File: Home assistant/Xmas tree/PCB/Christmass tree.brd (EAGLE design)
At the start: 64 x 38 mm, 12 parts, among them T1 BC547, X1 3PIN_5MM_TERMINAL

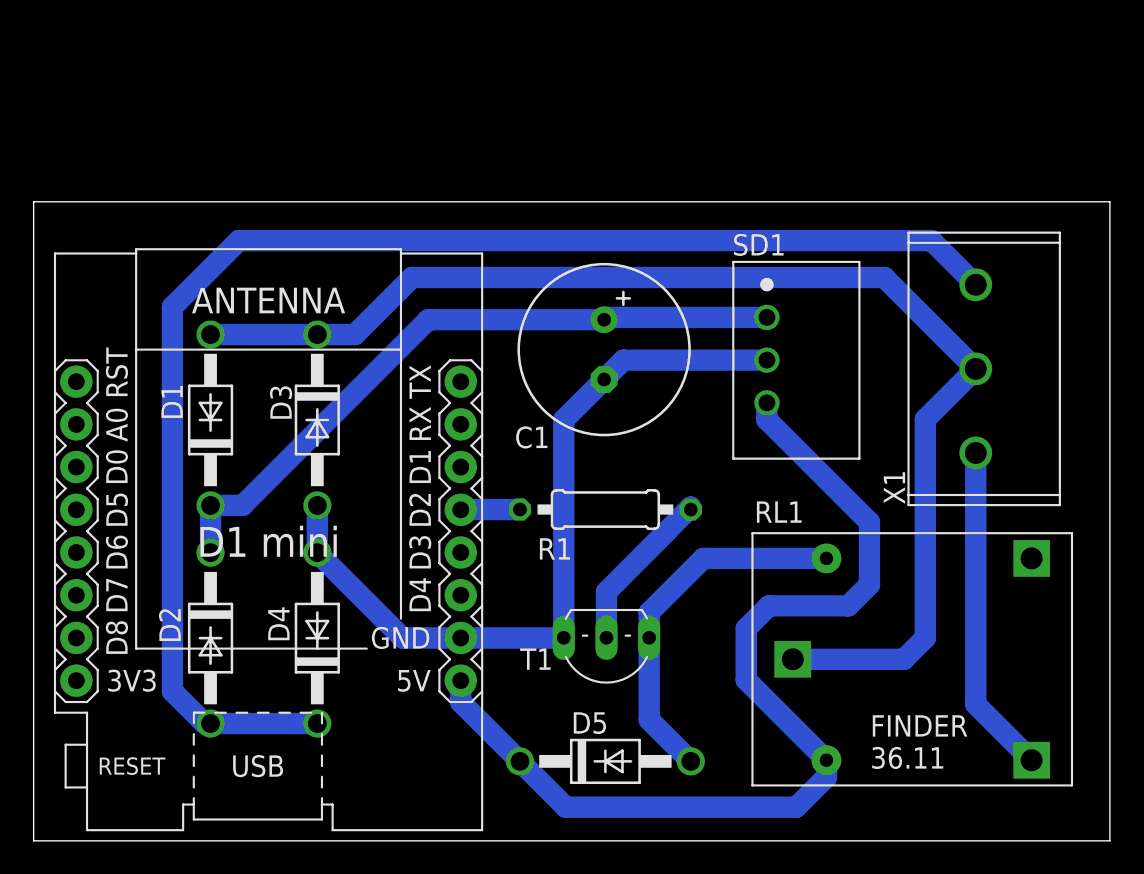
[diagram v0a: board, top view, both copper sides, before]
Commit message: Triac christmass tree
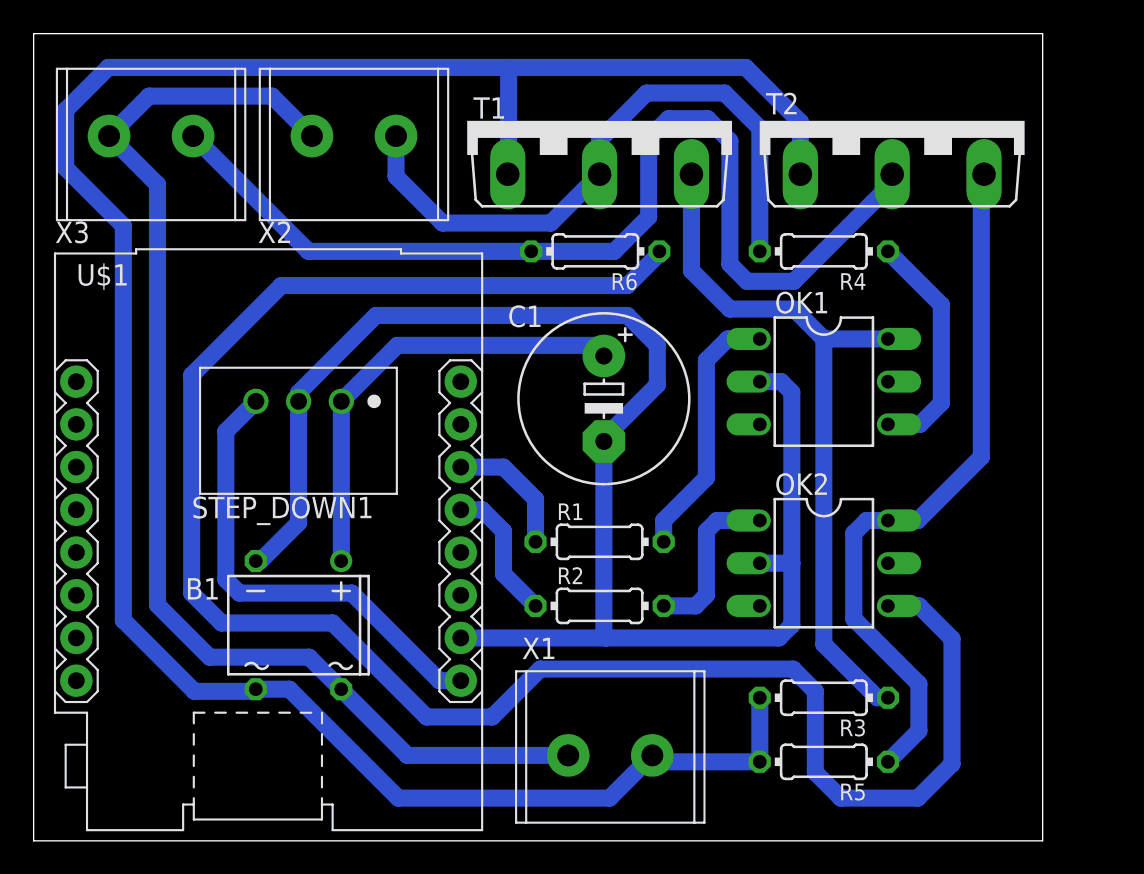
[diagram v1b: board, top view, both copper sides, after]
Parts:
- removed D1, D2, D3, D4, D5: 1N4004, diode:DO41-10
- removed RL1: 36.11, Rele_Finder:36.11
- removed SD1: TRACO_TSR_1-2450, Voltage:TRACO_TSR_1-2450
- added B1: DB107, rectifier:DB
- added OK1, OK2: MOC3022, optocoupler:DIL06
- added R2, R3, R4, R5, R6: 330R, resistor:0204/7
- added STEP_DOWN1: TRACO_TSR_1-2450, Voltage:TRACO_TSR_1-2450
- added T2: BTA10, triac:TO218DS
- added X2, X3: 2PIN_5MM_TERMINAL, Terminaly:2PIN_5MM_TERMMINAL
- C1: value 1000uF -> 470uF; device resistor:E3,5-10 -> resistor:E5-10,5
- R1: value 470R -> 330R; device resistor:0207/10 -> resistor:0204/7
- T1: value BC547 -> BTA10; device transistor:TO92-CBE -> triac:TO218DS
- U$1: device Sbirka modulu:WEMOS-D1-MINI -> Sbirka modulu:WEMOS-D1-MINI_BEZ
- X1: value 3PIN_5MM_TERMINAL -> 2PIN_5MM_TERMINAL; device Terminaly:3PIN_5MM_TERMINAL -> Terminaly:2PIN_5MM_TERMMINAL
- moved X1 31.6 mm to (34.3, 5.08), turned to 0 degrees
- moved T1 30.7 mm to (33.7, 42.8), turned to 0 degrees
- moved C1 2.92 mm to (33.9, 26.3)
- moved R1 1.95 mm to (33.7, 17.8)
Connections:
- removed net +12VAC: D1.A, D3.C, RL1.11, X1.2
- removed net -12VAC: D2.A, D4.C, X1.1
- removed net 12VDC: C1.+, D1.C, D2.C, SD1.VIN
- removed net OUTPUT: RL1.14, X1.3
- new net N$10: R4.2, T1.A2, X2.1
- new net N$13: OK2.4, R6.1
- new net N$14: R6.2, T2.A2, X3.1
- new net N$2: OK2.1, R2.1
- new net N$3: B1.+, C1.+, STEP_DOWN1.VIN
- new net N$7: OK1.6, R3.1, T1.G
- new net N$8: OK2.6, R5.1, T2.G
- new net N$9: OK1.4, R4.1
- new net V+: B1.AC1, R3.2, R5.2, T1.A1, T2.A1, X1.2
- new net V-: B1.AC2, X1.1, X2.2, X3.2
- net +5V: now also STEP_DOWN1.VOUT; no longer D5.C, RL1.A1, SD1.VOUT
- net GND: now also B1.-, OK1.2, OK2.2, STEP_DOWN1.GND; no longer D3.A, D4.A, SD1.GND, T1.E
- net N$4: now also R2.2, U$1.JP2.4; no longer R1.2, T1.B
- net N$5: now also R1.1, U$1.JP2.3; no longer D5.A, RL1.A2, T1.C
- net N$6: now also OK1.1, R1.2; no longer R1.1, U$1.JP2.4
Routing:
- net V+: track 0.00 -> 134.7 mm
- net N$13: track 0.00 -> 112.2 mm
- net -12VAC: track 82.8 -> 0.00 mm
- net +12VAC: track 74.8 -> 0.00 mm
- net V-: track 0.00 -> 71.2 mm
- net N$14: track 0.00 -> 61.7 mm
- net GND: track 46.1 -> 91.9 mm
- net N$7: track 0.00 -> 42.4 mm
- net N$8: track 0.00 -> 42.3 mm
- net 12VDC: track 40.5 -> 0.00 mm
- net N$10: track 0.00 -> 37.8 mm
- net +5V: track 58.9 -> 27.8 mm
- net N$3: track 0.00 -> 26.8 mm
- net OUTPUT: track 19.6 -> 0.00 mm
- net N$9: track 0.00 -> 14.0 mm
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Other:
- board size 64 x 38 mm -> 60 x 48 mm
